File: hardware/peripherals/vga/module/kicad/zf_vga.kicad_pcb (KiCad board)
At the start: 2 copper layers, 143 x 85 mm, 58 parts, among them J2 Z-FIGHTER Expansion Port, SW1 SW_DIP_x03, U1 4040, U10 74HC165, U11 AS6C6264, U12 74HC541, U13 74HC541, U14 74HC541, U2 4040, U3 GAL16V8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

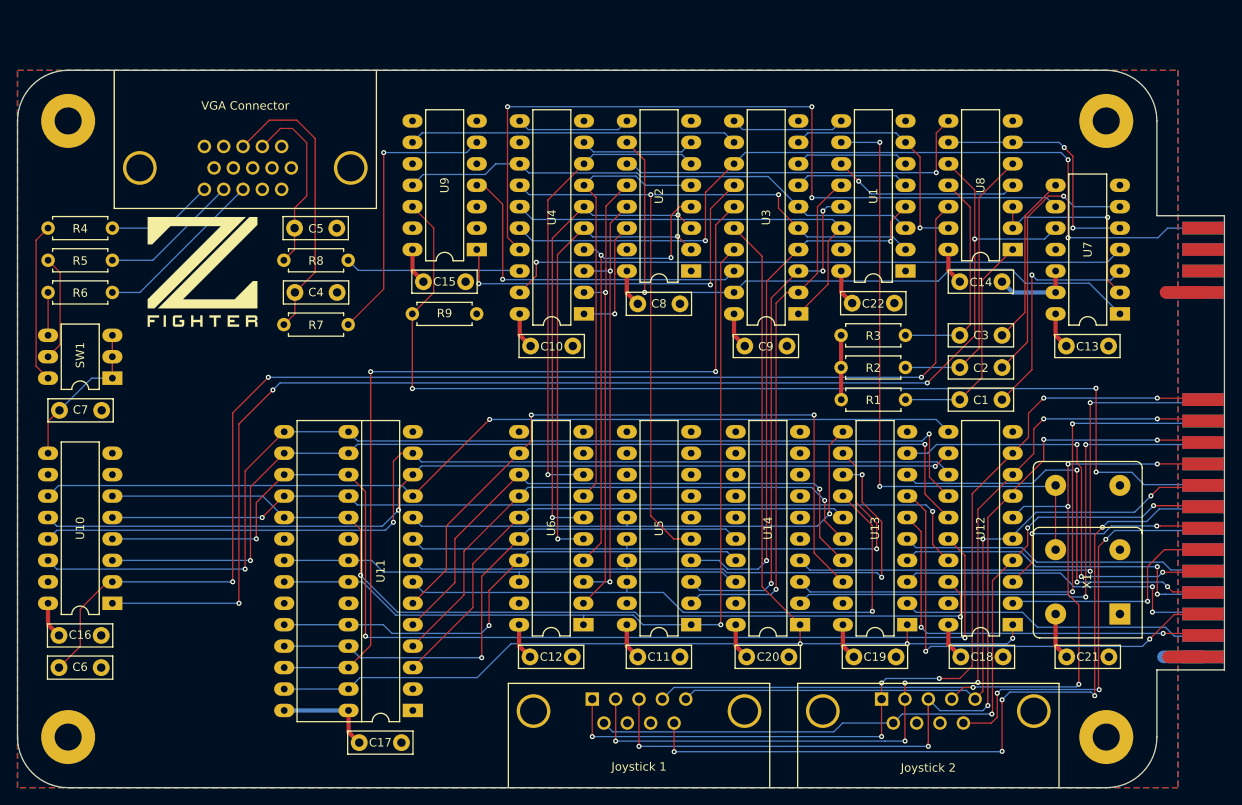
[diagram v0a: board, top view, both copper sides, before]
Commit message: VGA Rev. 2
Fixed VGA connector footprint, expanded joystick connectors for '241 buffer, added jumper-selectable interrupt generator
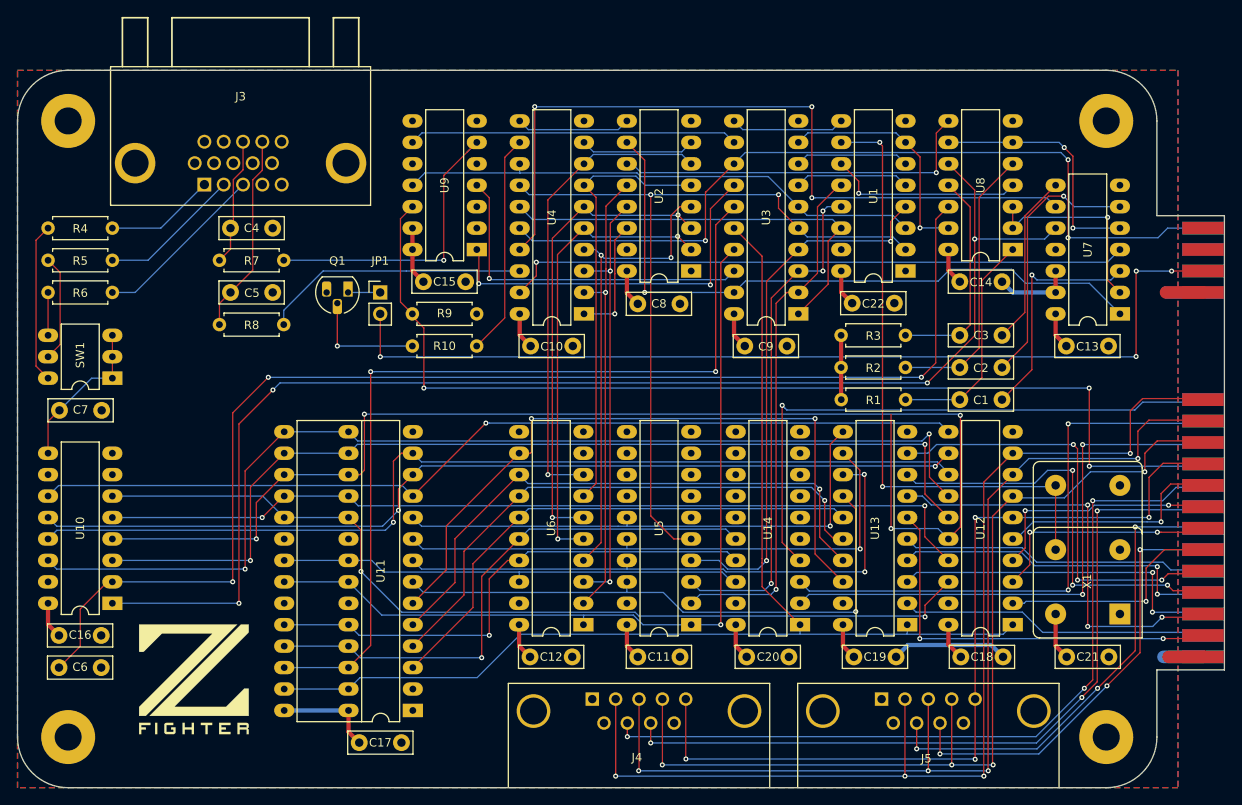
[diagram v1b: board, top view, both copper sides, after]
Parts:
- removed VGA Connector: DB15_Female, zf_vga:AHDF15A-KG-TAXB
- added ?: , , F.Cu at (133.1, 20.2)
- added J3: DB15_Female, zf_vga:L77HDE15SD1CH4FVGA, F.Cu at (108.8, 38.0)
- added JP1: Jumper, Connector_PinHeader_2.54mm:PinHeader_1x02_P2.54mm_Vertical, F.Cu at (129.6, 50.8)
- added Q1: BC547, Package_TO_SOT_THT:TO-92_HandSolder, F.Cu at (125.8, 50.8)
- added R10: 1K, Resistor_THT:R_Axial_DIN0207_L6.3mm_D2.5mm_P7.62mm_Horizontal, F.Cu at (141.0, 57.2)
- J4: renamed from Joystick 1
- J5: renamed from Joystick 2
- R1, R2: value R -> 220
- R3: value R -> 200
- moved G*** 48.3 mm to (107.5, 96.7)
- moved R7 10.8 mm to (118.2, 47.0)
- moved R8 10.8 mm to (118.2, 54.6)
- moved C4 10.8 mm to (116.9, 43.2)
- moved C5 10.8 mm to (111.9, 50.8)
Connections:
- J2 pad 12: Net-(J2-Pad12) -> PC7
- J2 pad 18: DATARDY -> PC4
- J2 pad 20: Net-(J2-Pad20) -> DATARDY
- J2 pad 29: Net-(J2-Pad29) -> #INT
- J4 pad 1: PA0 -> VCC
- J4 pad 2: PA1 -> PA0
- J4 pad 3: PA2 -> PA1
- J4 pad 4: PA3 -> PA2
- J4 pad 5: PA4 -> PA3
- J4 pad 6: PA5 -> GND
- J4 pad 7: VCC -> PC4
- J4 pad 8: GND -> PC5
- J4 pad 9: PC5 -> Net-(J4-Pad9)
- J5 pad 1: PA0 -> VCC
- J5 pad 2: PA1 -> PA0
- J5 pad 3: PA2 -> PA1
- J5 pad 4: PA3 -> PA2
- J5 pad 5: PA4 -> PA3
- J5 pad 6: PA5 -> GND
- J5 pad 7: VCC -> PC6
- J5 pad 8: GND -> PC7
- J5 pad 9: PC6 -> Net-(J5-Pad9)
- U4 pad 12: Net-(U4-Pad12) -> VSYNC
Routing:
- net #INT: track 0.00 -> 112.7 mm, vias 0 -> 4
- net PC4: track 0.00 -> 94.6 mm, vias 0 -> 3
- net PA5: track 93.0 -> 28.0 mm, vias 3 -> 2
- net PA4: track 83.4 -> 27.6 mm, vias 2 -> 1
- net PC7: track 0.00 -> 52.0 mm, vias 0 -> 3
- net VSYNC: track 0.00 -> 26.2 mm
- net PA0: track 108.9 -> 130.6 mm, vias 6 -> 4
- net Net-(C4-Pad2): track 34.4 -> 14.8 mm
- net Net-(Q1-Pad2): track 0.00 -> 13.9 mm, vias 0 -> 1
- net GND: track 26.6 -> 40.4 mm
- net PA1: track 108.4 -> 122.0 mm, vias 6 -> 4
- net D5: track 137.3 -> 149.3 mm, vias 3 -> 4
- net #VSYNC: track 20.8 -> 31.6 mm
- net PC6: track 49.7 -> 56.6 mm
- net PA2: track 108.3 -> 115.0 mm, vias 5 -> 4
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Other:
- board text added: "Z-FIGHTER VGA Module Rev. 2 @tangent3D 2022"
- board text removed: "Z-FIGHTER VGA Module Rev. 1 @tangent3D 2022"

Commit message: Routing
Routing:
- net #HSYNC: track 36.8 -> 35.2 mm
- net L6: track 55.6 -> 56.3 mm

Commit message: Silkscreen
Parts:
- moved G*** 3.53 mm to (107.5, 100.2)
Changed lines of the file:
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@@
   )
   (module zf_vga:Z-FIGHTER_Logo (layer F.Cu)
-    (at 107.524 96.654)
+    (at 107.524 100.186599)
     (fp_text reference G*** (at 0 0) (layer F.SilkS) hide
       (effects (font (size 1.524 1.524) (thickness 0.3)))
@@
       (effects (font (size 1.524 1.524) (thickness 0.3)))
     )
-    (fp_poly (pts (xy -5.147733 5.418667) (xy -6.231466 5.418667) (xy -6.231466 5.6896) (xy -5.6896 5.6896)
-      (xy -5.6896 5.960533) (xy -6.231466 5.960533) (xy -6.231466 6.5024) (xy -6.5024 6.5024)
-      (xy -6.5024 5.147733) (xy -5.147733 5.147733) (xy -5.147733 5.418667)) (layer F.SilkS) (width 0.01))
-    (fp_poly (pts (xy -4.334933 6.5024) (xy -4.605867 6.5024) (xy -4.605867 5.147733) (xy -4.334933 5.147733)
-      (xy -4.334933 6.5024)) (layer F.SilkS) (width 0.01))
+    (fp_poly (pts (xy 6.5024 -5.562624) (xy 2.095512 -1.155712) (xy -2.311375 3.2512) (xy 3.801633 3.2512)
+      (xy 5.968901 1.083734) (xy 6.5024 1.083734) (xy 6.5024 4.334934) (xy -5.274713 4.334934)
+      (xy 0.143934 -1.083733) (xy 5.56258 -6.5024) (xy 6.5024 -6.5024) (xy 6.5024 -5.562624)) (layer F.SilkS) (width 0.01))
+    (fp_poly (pts (xy -5.698047 4.334934) (xy -6.5024 4.334934) (xy -6.5024 3.259692) (xy -2.163246 -1.079487)
+      (xy 2.175909 -5.418666) (xy -3.801632 -5.418666) (xy -4.885267 -4.334933) (xy -5.968901 -3.2512)
+      (xy -6.5024 -3.2512) (xy -6.5024 -6.5024) (xy 5.139247 -6.5024) (xy -5.698047 4.334934)) (layer F.SilkS) (width 0.01))
+    (fp_poly (pts (xy 5.881374 5.147874) (xy 6.015819 5.148673) (xy 6.123625 5.150699) (xy 6.208404 5.15452)
+      (xy 6.273769 5.160703) (xy 6.323334 5.169816) (xy 6.360711 5.182428) (xy 6.389514 5.199105)
+      (xy 6.413357 5.220416) (xy 6.435852 5.246928) (xy 6.447986 5.262658) (xy 6.468737 5.292787)
+      (xy 6.482467 5.323556) (xy 6.491023 5.363377) (xy 6.496249 5.42066) (xy 6.49981 5.498917)
+      (xy 6.506358 5.675819) (xy 6.359882 5.825067) (xy 6.431141 5.897674) (xy 6.5024 5.970282)
+      (xy 6.5024 6.5024) (xy 6.231467 6.5024) (xy 6.231467 5.960533) (xy 5.418667 5.960533)
+      (xy 5.418667 6.5024) (xy 5.147733 6.5024) (xy 5.147733 5.418667) (xy 5.418667 5.418667)
+      (xy 5.418667 5.6896) (xy 6.231467 5.6896) (xy 6.231467 5.418667) (xy 5.418667 5.418667)
+      (xy 5.147733 5.418667) (xy 5.147733 5.147733) (xy 5.716674 5.147733) (xy 5.881374 5.147874)) (layer F.SilkS) (width 0.01))
+    (fp_poly (pts (xy 4.334934 5.418667) (xy 3.2512 5.418667) (xy 3.2512 5.6896) (xy 3.793067 5.6896)
+      (xy 3.793067 5.960533) (xy 3.2512 5.960533) (xy 3.2512 6.231467) (xy 4.334934 6.231467)
+      (xy 4.334934 6.5024) (xy 2.980267 6.5024) (xy 2.980267 5.147733) (xy 4.334934 5.147733)
+      (xy 4.334934 5.418667)) (layer F.SilkS) (width 0.01))
+    (fp_poly (pts (xy 2.167467 5.418667) (xy 1.6256 5.418667) (xy 1.6256 6.5024) (xy 1.354667 6.5024)
+      (xy 1.354667 5.418667) (xy 0.8128 5.418667) (xy 0.8128 5.147733) (xy 2.167467 5.147733)
+      (xy 2.167467 5.418667)) (layer F.SilkS) (width 0.01))
+    (fp_poly (pts (xy -1.083733 5.6896) (xy -0.270933 5.6896) (xy -0.270933 5.147733) (xy 0 5.147733)
+      (xy 0 6.5024) (xy -0.270933 6.5024) (xy -0.270933 5.960533) (xy -1.083733 5.960533)
+      (xy -1.083733 6.5024) (xy -1.354667 6.5024) (xy -1.354667 5.147733) (xy -1.083733 5.147733)
+      (xy -1.083733 5.6896)) (layer F.SilkS) (width 0.01))
     (fp_poly (pts (xy -2.4384 5.418667) (xy -3.2512 5.418667) (xy -3.2512 6.231467) (xy -2.4384 6.231467)
       (xy -2.4384 5.960533) (xy -2.709333 5.960533) (xy -2.709333 5.6896) (xy -2.167466 5.6896)
@@
       (xy -3.01757 5.148068) (xy -2.872322 5.147734) (xy -2.871874 5.147733) (xy -2.4384 5.147733)
       (xy -2.4384 5.418667)) (layer F.SilkS) (width 0.01))
-    (fp_poly (pts (xy -1.083733 5.6896) (xy -0.270933 5.6896) (xy -0.270933 5.147733) (xy 0 5.147733)
-      (xy 0 6.5024) (xy -0.270933 6.5024) (xy -0.270933 5.960533) (xy -1.083733 5.960533)
-      (xy -1.083733 6.5024) (xy -1.354667 6.5024) (xy -1.354667 5.147733) (xy -1.083733 5.147733)
-      (xy -1.083733 5.6896)) (layer F.SilkS) (width 0.01))
-    (fp_poly (pts (xy 2.167467 5.418667) (xy 1.6256 5.418667) (xy 1.6256 6.5024) (xy 1.354667 6.5024)
-      (xy 1.354667 5.418667) (xy 0.8128 5.418667) (xy 0.8128 5.147733) (xy 2.167467 5.147733)
-      (xy 2.167467 5.418667)) (layer F.SilkS) (width 0.01))
-    (fp_poly (pts (xy 4.334934 5.418667) (xy 3.2512 5.418667) (xy 3.2512 5.6896) (xy 3.793067 5.6896)
-      (xy 3.793067 5.960533) (xy 3.2512 5.960533) (xy 3.2512 6.231467) (xy 4.334934 6.231467)
-      (xy 4.334934 6.5024) (xy 2.980267 6.5024) (xy 2.980267 5.147733) (xy 4.334934 5.147733)
-      (xy 4.334934 5.418667)) (layer F.SilkS) (width 0.01))
-    (fp_poly (pts (xy 5.881374 5.147874) (xy 6.015819 5.148673) (xy 6.123625 5.150699) (xy 6.208404 5.15452)
-      (xy 6.273769 5.160703) (xy 6.323334 5.169816) (xy 6.360711 5.182428) (xy 6.389514 5.199105)
-      (xy 6.413357 5.220416) (xy 6.435852 5.246928) (xy 6.447986 5.262658) (xy 6.468737 5.292787)
-      (xy 6.482467 5.323556) (xy 6.491023 5.363377) (xy 6.496249 5.42066) (xy 6.49981 5.498917)
-      (xy 6.506358 5.675819) (xy 6.359882 5.825067) (xy 6.431141 5.897674) (xy 6.5024 5.970282)
-      (xy 6.5024 6.5024) (xy 6.231467 6.5024) (xy 6.231467 5.960533) (xy 5.418667 5.960533)
-      (xy 5.418667 6.5024) (xy 5.147733 6.5024) (xy 5.147733 5.418667) (xy 5.418667 5.418667)
-      (xy 5.418667 5.6896) (xy 6.231467 5.6896) (xy 6.231467 5.418667) (xy 5.418667 5.418667)
-      (xy 5.147733 5.418667) (xy 5.147733 5.147733) (xy 5.716674 5.147733) (xy 5.881374 5.147874)) (layer F.SilkS) (width 0.01))
-    (fp_poly (pts (xy -5.698047 4.334934) (xy -6.5024 4.334934) (xy -6.5024 3.259692) (xy -2.163246 -1.079487)
-      (xy 2.175909 -5.418666) (xy -3.801632 -5.418666) (xy -4.885267 -4.334933) (xy -5.968901 -3.2512)
-      (xy -6.5024 -3.2512) (xy -6.5024 -6.5024) (xy 5.139247 -6.5024) (xy -5.698047 4.334934)) (layer F.SilkS) (width 0.01))
-    (fp_poly (pts (xy 6.5024 -5.562624) (xy 2.095512 -1.155712) (xy -2.311375 3.2512) (xy 3.801633 3.2512)
-      (xy 5.968901 1.083734) (xy 6.5024 1.083734) (xy 6.5024 4.334934) (xy -5.274713 4.334934)
-      (xy 0.143934 -1.083733) (xy 5.56258 -6.5024) (xy 6.5024 -6.5024) (xy 6.5024 -5.562624)) (layer F.SilkS) (width 0.01))
+    (fp_poly (pts (xy -4.334933 6.5024) (xy -4.605867 6.5024) (xy -4.605867 5.147733) (xy -4.334933 5.147733)
+      (xy -4.334933 6.5024)) (layer F.SilkS) (width 0.01))
+    (fp_poly (pts (xy -5.147733 5.418667) (xy -6.231466 5.418667) (xy -6.231466 5.6896) (xy -5.6896 5.6896)
+      (xy -5.6896 5.960533) (xy -6.231466 5.960533) (xy -6.231466 6.5024) (xy -6.5024 6.5024)
+      (xy -6.5024 5.147733) (xy -5.147733 5.147733) (xy -5.147733 5.418667)) (layer F.SilkS) (width 0.01))
   )
   (module Connector_Dsub:DSUB-9_Male_Horizontal_P2.77x2.84mm_EdgePinOffset7.70mm_Housed_MountingHolesOffset9.12mm (layer F.Cu)
@@
       (effects (font (size 1 1) (thickness 0.15)))
     )
+    (fp_text user %R (at 0.3 0) (layer F.Fab)
+      (effects (font (size 1 1) (thickness 0.15)))
+    )
+    (fp_circle (center 0 0) (end 3.2 0) (layer Cmts.User) (width 0.15))
     (fp_circle (center 0 0) (end 3.45 0) (layer F.CrtYd) (width 0.05))
-    (fp_circle (center 0 0) (end 3.2 0) (layer Cmts.User) (width 0.15))
-    (fp_text user %R (at 0.3 0) (layer F.Fab)
-      (effects (font (size 1 1) (thickness 0.15)))
-    )
     (pad 1 thru_hole circle (at 0 0) (size 6.4 6.4) (drill 3.200001) (layers *.Cu *.Mask))
   )
